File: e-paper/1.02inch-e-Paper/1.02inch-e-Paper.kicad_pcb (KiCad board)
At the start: 2 copper layers, 40 x 20.9 mm, 23 parts, among them J1 Conn_01x06_Pin, J2 Conn_01x03_Pin

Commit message: update e-paper
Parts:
- C10, C11, C12, C13, C14, C3, C5, C6, C7, C8, C9, FPC1: moved to F.Cu
- moved C14 22.2 mm to (9.29, -8.00), turned to 180 degrees
- moved C3 22.2 mm to (9.29, 7.99)
- moved C13 20.1 mm to (9.29, -6.40), turned to 180 degrees
- moved C5 20.0 mm to (9.29, 6.39)
- moved C4 19.6 mm to (9.29, 8.00)
- moved C17 19.6 mm to (9.29, -8.00)
- moved C12 18.2 mm to (9.29, -4.80), turned to 180 degrees
- moved C6 18.2 mm to (9.29, 4.80)
- moved FPC1 17.2 mm to (14.8, 0.00), turned to 90 degrees
- moved C1 17.1 mm to (9.29, 6.40)
- moved C16 17.1 mm to (9.29, -6.40)
- moved C11 16.7 mm to (9.29, -3.20), turned to 180 degrees
- moved C7 16.7 mm to (9.29, 3.20)
- moved C10 15.8 mm to (9.29, -1.60), turned to 180 degrees
- moved C8 15.8 mm to (9.29, 1.60)
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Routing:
- net DC: track 27.9 -> 14.9 mm
- net RST: track 28.7 -> 15.8 mm
- net CS: track 27.0 -> 16.1 mm
- net DIN: track 25.6 -> 15.1 mm
- net CLK: track 26.3 -> 16.4 mm
- net 3.3V: track 38.8 -> 30.3 mm, vias 2 -> 1
- net GND: track 90.4 -> 98.1 mm
- net Net-(C14-Pad1): track 8.28 -> 4.29 mm
- net Net-(C13-Pad1): track 8.04 -> 4.05 mm
- net Net-(C12-Pad1): track 7.79 -> 3.80 mm
- net Net-(C11-Pad1): track 7.54 -> 3.60 mm
- net Net-(C10-Pad1): track 7.29 -> 3.42 mm
- net Net-(C9-Pad1): track 7.04 -> 3.67 mm
- net Net-(C3-Pad1): track 13.6 -> 10.2 mm, vias 0 -> 1
- net Net-(C15-Pad2): track 10.1 -> 8.09 mm, vias 2 -> 1
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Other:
- board size 40 x 20.9 mm -> 60 x 20.9 mm

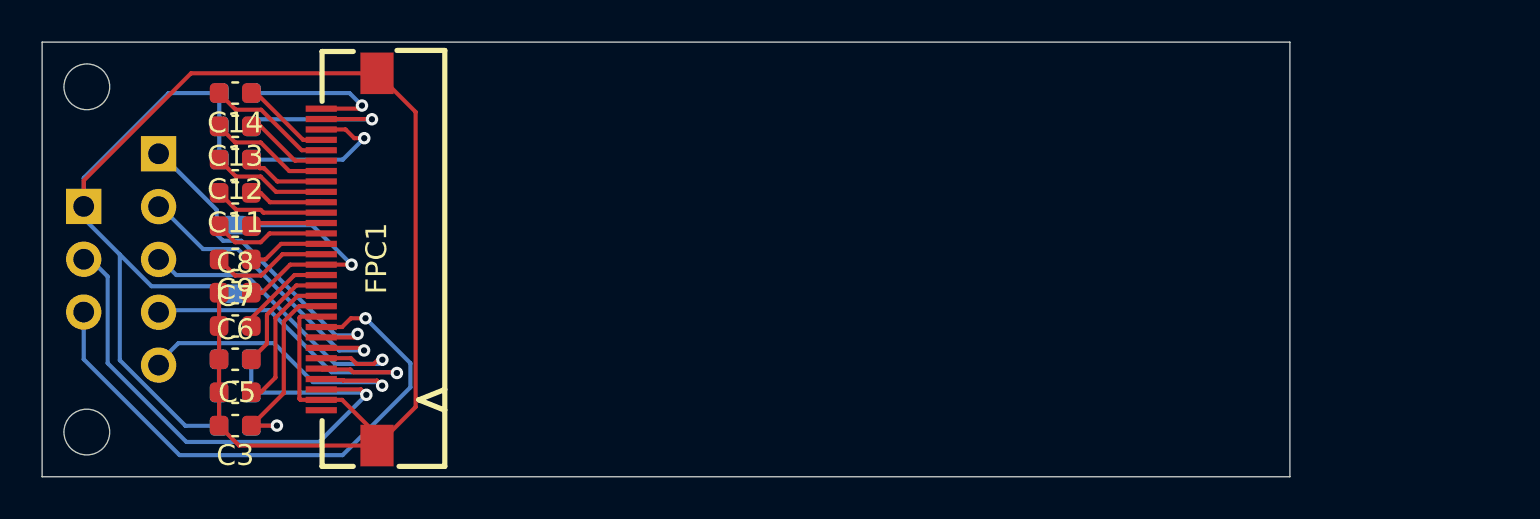
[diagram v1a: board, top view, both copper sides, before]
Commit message: add country yard to power swith
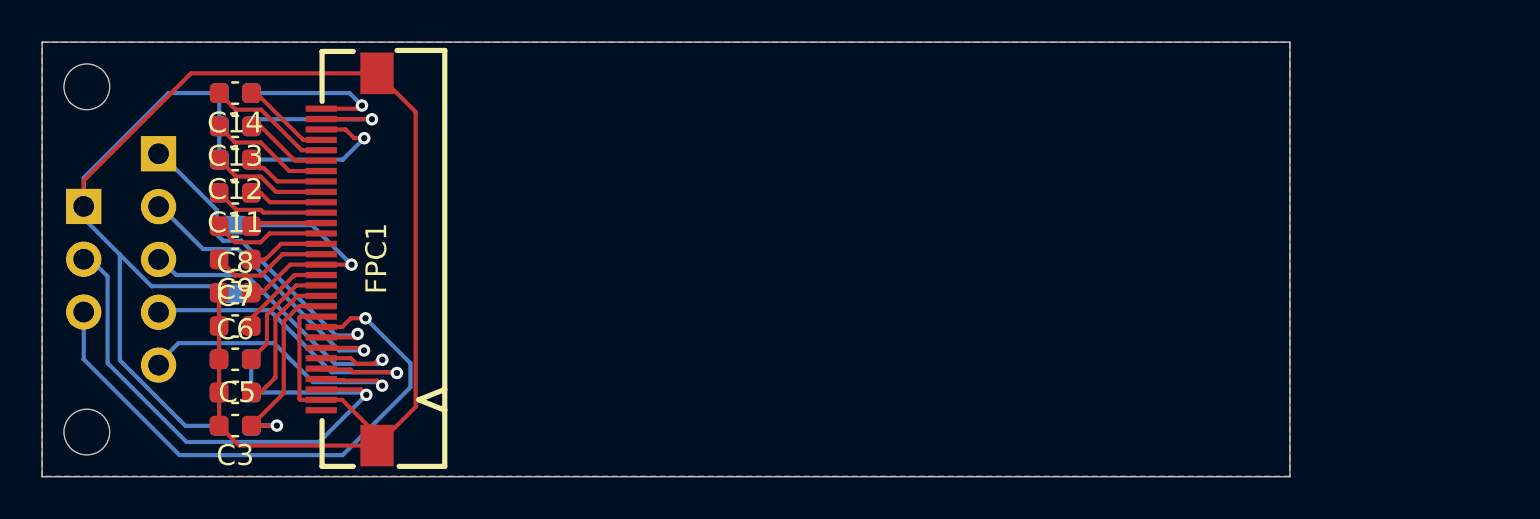
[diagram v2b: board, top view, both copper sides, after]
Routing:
- added copper zone on B.Cu, net GND
- added copper zone on F.Cu, net GND
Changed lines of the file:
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@@
 		(net 29)
+	)
+	(zone
+		(net 1)
+		(net_name "GND")
+		(layers "F.Cu" "B.Cu")
+		(hatch edge 0.5)
+		(connect_pads
+			(clearance 0.5)
+		)
+		(min_thickness 0.25)
+		(filled_areas_thickness no)
+		(fill yes
+			(thermal_gap 0.5)
+			(thermal_bridge_width 0.5)
+		)
+		(polygon
+			(pts
+				(xy 0.01 -10.44) (xy 60 -10.44) (xy 60 10.42) (xy 59.99 10.43) (xy 0 10.43) (xy 0 -10.43)
+			)
+		)
 	)
 	(embedded_fonts no)

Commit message: add RGB led in e-paper module
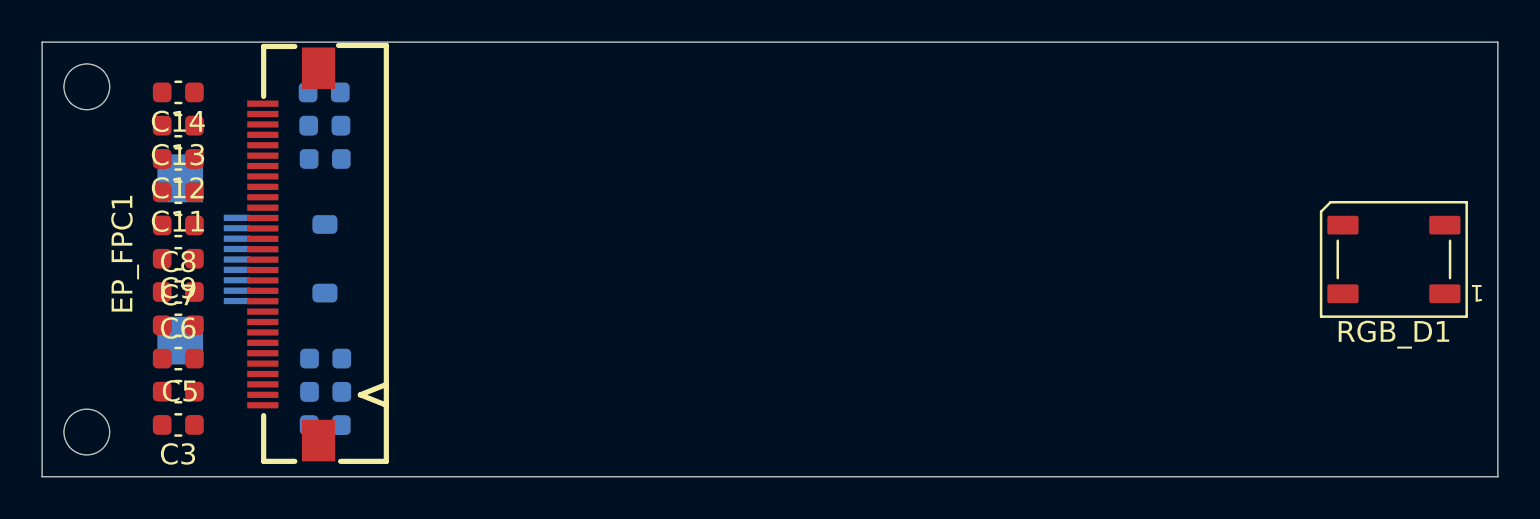
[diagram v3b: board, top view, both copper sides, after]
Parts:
- removed FPC1: AFC01-S30FCA-00, ErgoCai.pretty:FPC-SMD_AFC01-S30FCA-00
- removed J1: Conn_01x06_Pin, Connector_PinHeader_2.54mm:PinHeader_1x05_P2.54mm_Vertical
- removed J2: Conn_01x03_Pin, Connector_PinHeader_2.54mm:PinHeader_1x03_P2.54mm_Vertical
- added EP_FPC1: AFC01-S30FCA-00, ErgoCai.pretty:FPC-SMD_AFC01-S30FCA-00, F.Cu at (12.0, -0.24)
- added EP_FPC2: AFD01-S09FCA-00, ErgoCai.pretty:FPC-SMD_9P-P0.50_JS_AFD01-S09FCA-00, B.Cu at (8.00, 0.00)
- added RGB_D1: WS2812B, ErgoCai.pretty:LED_WS2812B_PLCC4_5.0x5.0mm_P3.2mm, F.Cu at (65.0, 0.00)
- moved C2 4.36 mm to (13.6, 4.77)
- moved C1 4.35 mm to (13.6, 6.37)
- moved C4 4.33 mm to (13.6, 7.97)
- moved C15 4.32 mm to (13.6, -4.83)
- moved D1 4.31 mm to (13.6, -0.03)
- moved C16 4.30 mm to (13.6, -6.43)
- moved C17 4.27 mm to (13.6, -8.03)
- moved C10 2.74 mm to (6.55, -1.63)
- moved C11 2.74 mm to (6.55, -3.23)
- moved C12 2.74 mm to (6.55, -4.83)
- moved C13 2.74 mm to (6.55, -6.43)
- moved C14 2.74 mm to (6.55, -8.03)
- moved C3 2.74 mm to (6.55, 7.96)
- moved C5 2.74 mm to (6.55, 6.36)
- moved C6 2.74 mm to (6.55, 4.77)
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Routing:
- net GND: track 98.1 -> 0.00 mm
- net 3.3V: track 30.3 -> 0.00 mm, vias 1 -> 0
- net BUSY: track 28.1 -> 0.00 mm, vias 1 -> 0
- net CLK: track 16.4 -> 0.00 mm, vias 1 -> 0
- net CS: track 16.1 -> 0.00 mm, vias 1 -> 0
- net RST: track 15.8 -> 0.00 mm, vias 1 -> 0
- net DIN: track 15.1 -> 0.00 mm, vias 1 -> 0
- net DC: track 14.9 -> 0.00 mm, vias 1 -> 0
- net Net-(D1-A): track 11.8 -> 0.00 mm, vias 1 -> 0
- net Net-(C3-Pad1): track 10.2 -> 0.00 mm, vias 1 -> 0
- net Net-(C16-Pad2): track 8.37 -> 0.00 mm, vias 1 -> 0
- net Net-(C15-Pad2): track 8.09 -> 0.00 mm, vias 1 -> 0
- net Net-(C17-Pad2): track 7.58 -> 0.00 mm, vias 1 -> 0
- net Net-(C5-Pad2): track 6.96 -> 0.00 mm
- net Net-(C14-Pad2): track 6.05 -> 0.00 mm
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- removed copper zone on B.Cu, net GND
- removed copper zone on F.Cu, net GND
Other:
- board size 60 x 20.9 mm -> 70 x 20.9 mm
